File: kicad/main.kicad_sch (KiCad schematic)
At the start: 35 parts, among them J1 Jack-DC, J2 LCD_Out, J3 LCD_Light, J4 VIA_A, J5 VIA_B, J6 VIA_Power, SW1 Step, SW2 Reset, X1 1 MHz

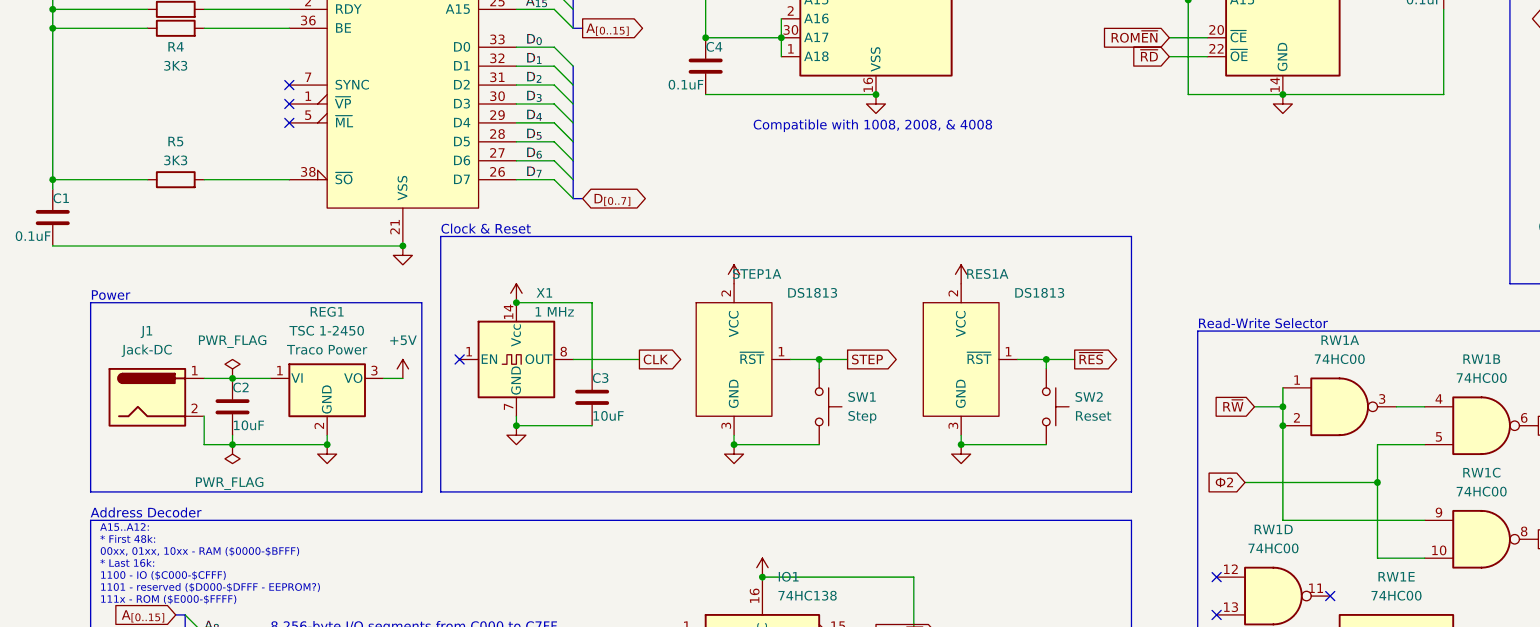
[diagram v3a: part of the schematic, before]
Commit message: Add LEDs
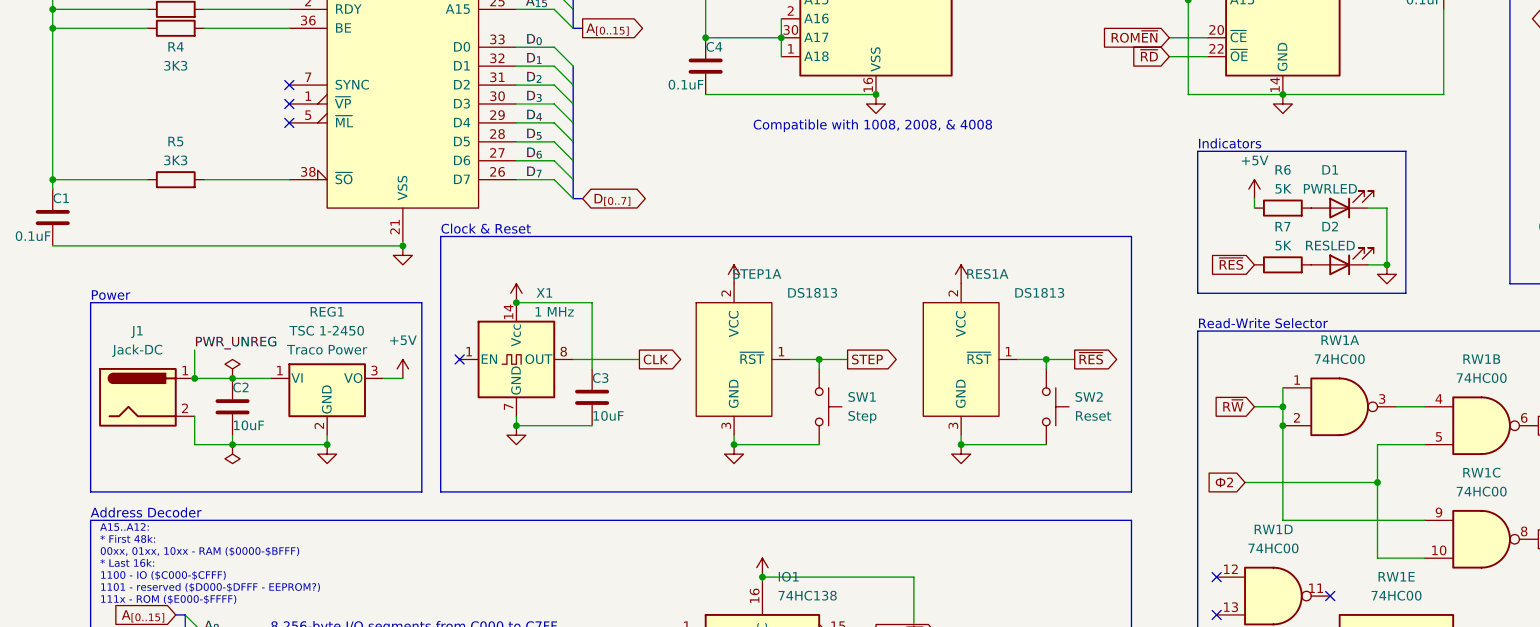
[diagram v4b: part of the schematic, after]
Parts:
- added D1: PWRLED, LED_THT:LED_D3.0mm, symbol Device:LED
- added D2: RESLED, LED_THT:LED_D3.0mm, symbol Device:LED
- added R6, R7: 5K, Resistor_THT:R_Axial_DIN0204_L3.6mm_D1.6mm_P7.62mm_Horizontal, symbol Device:R
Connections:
- net +5V: now also R6.1
- net GND: now also D1.1 (K), D2.1 (K)
- net ~{RES}: now also R7.1
- net PWR_UNREG: now reaches C2.1, J1.1, REG1.1 (VI)
- new net: D1.2 (A), R6.2
- new net: D2.2 (A), R7.2
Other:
- note added: "Indicators"
- moved on the sheet: J1

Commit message: V08
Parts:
- removed J2: LCD_Out, Connector_PinHeader_2.54mm:PinHeader_1x14_P2.54mm_Vertical, symbol Connector:Conn_01x14_Male
- removed J3: LCD_Light, Connector_PinHeader_2.54mm:PinHeader_1x02_P2.54mm_Vertical, symbol Connector:Conn_01x02_Male
- removed J4: VIA_A, Connector_PinHeader_2.54mm:PinHeader_2x05_P2.54mm_Vertical, symbol Connector:Conn_01x10_Male
- removed J5: VIA_B, Connector_PinHeader_2.54mm:PinHeader_2x05_P2.54mm_Vertical, symbol Connector:Conn_01x10_Male
- removed J6: VIA_Power, Connector_PinHeader_2.54mm:PinHeader_1x02_P2.54mm_Vertical, symbol Connector:Conn_01x02_Male
- added J2: LCD, Connector_PinHeader_2.54mm:PinHeader_1x16_P2.54mm_Vertical, symbol Connector:Conn_01x16_Male
- added J3: VIA_A, Connector_PinHeader_2.54mm:PinHeader_2x07_P2.54mm_Vertical, symbol Connector:Conn_01x14_Male
- added J4: VIA_B, Connector_PinHeader_2.54mm:PinHeader_2x07_P2.54mm_Vertical, symbol Connector:Conn_01x14_Male
- D1: value PWRLED -> PWR
- D2: value RESLED -> RES
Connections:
- net +5V: now also J2.15 (Pin_15), J2.2 (Pin_2), J3.14 (Pin_14), J3.2 (Pin_2), J4.14 (Pin_14), J4.2 (Pin_2)
- net A_{0}: now also J2.4 (Pin_4)
- net D_{0}: now also J2.7 (Pin_7)
- net D_{1}: now also J2.8 (Pin_8)
- net D_{2}: now also J2.9 (Pin_9)
- net D_{3}: now also J2.10 (Pin_10)
- net D_{4}: now also J2.11 (Pin_11)
- net D_{5}: now also J2.12 (Pin_12)
- net D_{6}: now also J2.13 (Pin_13)
- net D_{7}: now also J2.14 (Pin_14)
- net GND: now also J2.1 (Pin_1), J2.16 (Pin_16), J3.1 (Pin_1), J3.13 (Pin_13), J4.1 (Pin_1), J4.13 (Pin_13)
- net LCD~{EN}: now also J2.6 (Pin_6)
- net ~{WD}: now also J2.5 (Pin_5)
- net at RV1.2: now also J2.3 (Pin_3)
- net at VIA1.2 (PA0): now also J3.3 (Pin_3)
- net at VIA1.39 (CA2): now also J3.12 (Pin_12)
- net at VIA1.3 (PA1): now also J3.4 (Pin_4)
- net at VIA1.4 (PA2): now also J3.5 (Pin_5)
- net at VIA1.5 (PA3): now also J3.6 (Pin_6)
- net at VIA1.6 (PA4): now also J3.7 (Pin_7)
- net at VIA1.7 (PA5): now also J3.8 (Pin_8)
- net at VIA1.8 (PA6): now also J3.9 (Pin_9)
- net at VIA1.9 (PA7): now also J3.10 (Pin_10)
- net at VIA1.40 (CA1): now also J3.11 (Pin_11)
- net at VIA1.10 (PB0): now also J4.3 (Pin_3)
- net at VIA1.19 (CB2): now also J4.12 (Pin_12)
- net at VIA1.11 (PB1): now also J4.4 (Pin_4)
- net at VIA1.12 (PB2): now also J4.5 (Pin_5)
- net at VIA1.13 (PB3): now also J4.6 (Pin_6)
- net at VIA1.14 (PB4): now also J4.7 (Pin_7)
- net at VIA1.15 (PB5): now also J4.8 (Pin_8)
- net at VIA1.16 (PB6): now also J4.9 (Pin_9)
- net at VIA1.17 (PB7): now also J4.10 (Pin_10)
- net at VIA1.18 (CB1): now also J4.11 (Pin_11)

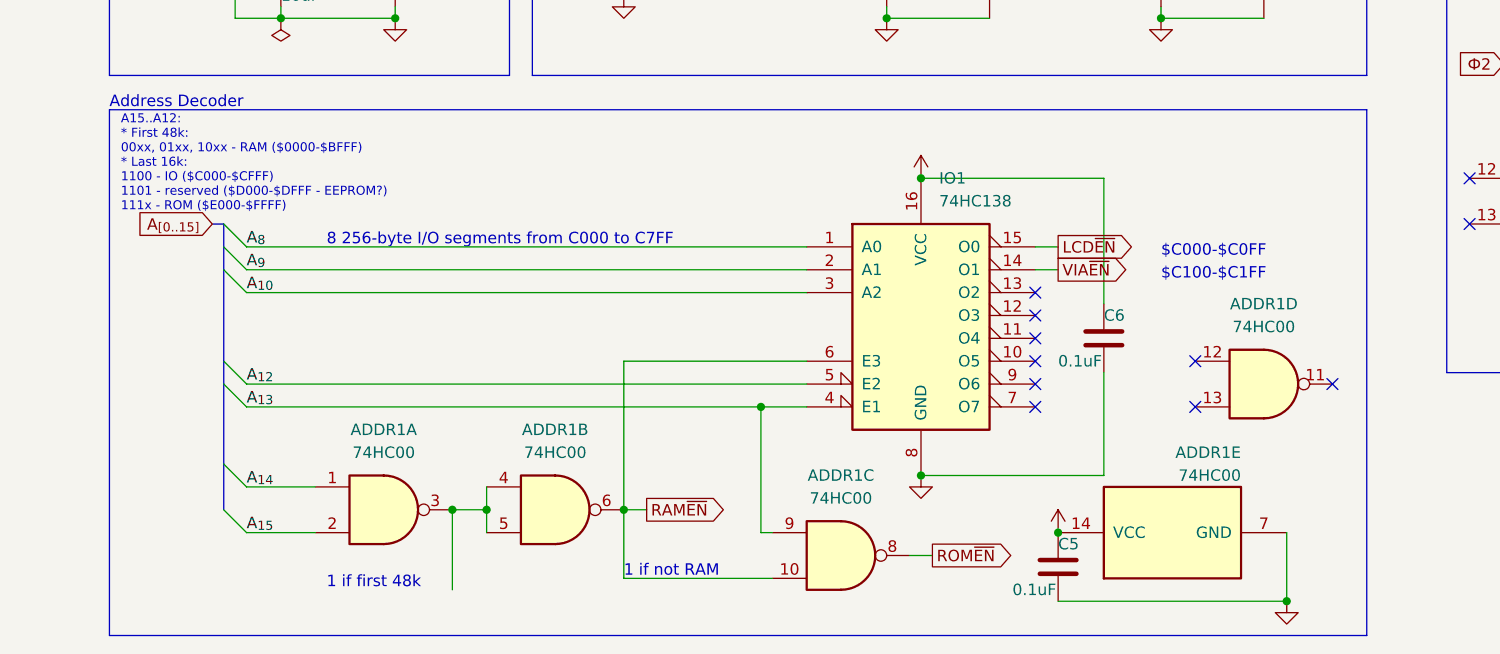
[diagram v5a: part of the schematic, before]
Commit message: Update V8 schematics, move I/O to $Dxxx
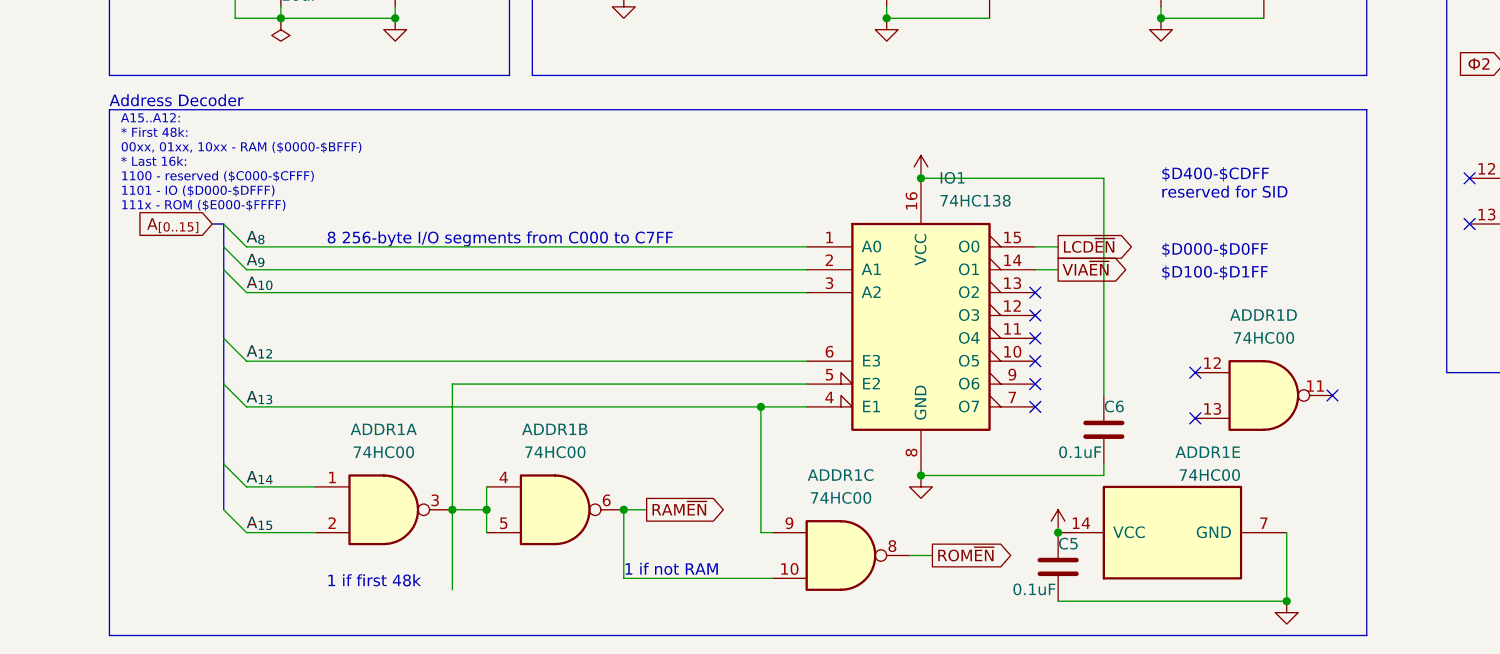
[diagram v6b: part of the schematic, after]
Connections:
- net A_{12}: now also IO1.6 (E3); no longer IO1.5 (E2)
- net RAM~{EN}: no longer IO1.6 (E3)
- net at ADDR1.3, ADDR1.4, ADDR1.5: now also IO1.5 (E2)
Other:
- note added: "$D000-$D0FF"
- note added: "$D100-$D1FF"
- note added: "$D400-$CDFF reserved for SID"
- note added: "A15..A12: * First 48k: 00xx, 01xx, 10xx - RAM ($0000-$BFFF) * Last 16k: 1100 - reserved ($C000-$CFFF) 1101 - IO ($D000-$DFFF) 111x - ROM ($E000-$FFFF)"
- note removed: "$C000-$C0FF"
- note removed: "$C100-$C1FF"
- note removed: "A15..A12: * First 48k: 00xx, 01xx, 10xx - RAM ($0000-$BFFF) * Last 16k: 1100 - IO ($C000-$CFFF) 1101 - reserved ($D000-$DFFF - EEPROM?) 111x - ROM ($E000-$FFFF)"
- moved on the sheet: ADDR1D, C6
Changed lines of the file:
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@@
   (no_connect (at 127 166.37))
   (no_connect (at 50.8 39.37))
-  (no_connect (at 160.02 166.37))
+  (no_connect (at 160.02 167.64))
   (no_connect (at 127 168.91))
-  (no_connect (at 144.78 163.83))
+  (no_connect (at 144.78 165.1))
   (no_connect (at 73.66 114.3))
   (no_connect (at 127 156.21))
   (no_connect (at 50.8 77.47))
-  (no_connect (at 144.78 168.91))
+  (no_connect (at 144.78 170.18))
   (no_connect (at 127 163.83))
   (no_connect (at 50.8 80.01))
@@
     (stroke (width 0) (type default) (color 0 0 0 0))
   )
-  (bus_entry (at 36.83 163.83) (size 2.54 2.54)
+  (bus_entry (at 36.83 161.29) (size 2.54 2.54)
     (stroke (width 0) (type default) (color 0 0 0 0))
   )
@@
     (stroke (width 0.75) (type default) (color 0 0 0 0))
   )
-  (wire (pts (xy 269.24 151.13) (xy 260.35 151.13))
+  (wire (pts (xy 62.23 166.37) (xy 62.23 180.34))
     (stroke (width 0) (type default) (color 0 0 0 0))
   )
-  (wire (pts (xy 81.28 163.83) (xy 81.28 180.34))
+  (wire (pts (xy 269.24 151.13) (xy 260.35 151.13))
     (stroke (width 0) (type default) (color 0 0 0 0))
   )
@@
     (stroke (width 0) (type default) (color 0 0 0 0))
   )
-  (wire (pts (xy 81.28 163.83) (xy 101.6 163.83))
-    (stroke (width 0) (type default) (color 0 0 0 0))
-  )
   (wire (pts (xy 234.95 53.34) (xy 229.87 53.34))
     (stroke (width 0) (type default) (color 0 0 0 0))
@@
     (stroke (width 0) (type default) (color 0 0 0 0))
   )
+  (wire (pts (xy 62.23 166.37) (xy 101.6 166.37))
+    (stroke (width 0) (type default) (color 0 0 0 0))
+  )
   (wire (pts (xy 96.52 182.88) (xy 97.79 182.88))
     (stroke (width 0) (type default) (color 0 0 0 0))
@@
     (stroke (width 0) (type default) (color 0 0 0 0))
   )
-  (wire (pts (xy 39.37 166.37) (xy 101.6 166.37))
+  (wire (pts (xy 39.37 163.83) (xy 101.6 163.83))
     (stroke (width 0) (type default) (color 0 0 0 0))
   )
@@
     (stroke (width 0) (type default) (color 0 0 0 0))
   )
-  (bus (pts (xy 36.83 163.83) (xy 36.83 166.37))
+  (bus (pts (xy 36.83 161.29) (xy 36.83 166.37))
     (stroke (width 0.75) (type default) (color 0 0 0 0))
   )
@@
     (stroke (width 0) (type default) (color 0 0 0 0))
   )
-  (wire (pts (xy 134.62 157.48) (xy 134.62 143.51))
+  (wire (pts (xy 134.62 167.64) (xy 134.62 143.51))
     (stroke (width 0) (type default) (color 0 0 0 0))
   )
@@
     (stroke (width 0) (type default) (color 0 0 0 0))
   )
-  (bus (pts (xy 36.83 153.67) (xy 36.83 163.83))
+  (bus (pts (xy 36.83 153.67) (xy 36.83 161.29))
     (stroke (width 0.75) (type default) (color 0 0 0 0))
   )
@@
     (stroke (width 0.75) (type default) (color 0 0 0 0))
   )
-  (wire (pts (xy 134.62 165.1) (xy 134.62 176.53))
+  (wire (pts (xy 134.62 175.26) (xy 134.62 176.53))
     (stroke (width 0) (type default) (color 0 0 0 0))
   )
@@
     (effects (font (size 1.27 1.27)) (justify left bottom))
   )
-  (text "$C100-$C1FF" (at 140.97 154.94 0)
+  (text "$D100-$D1FF" (at 140.97 154.94 0)
     (effects (font (size 1.27 1.27)) (justify left bottom))
   )
-  (text "A15..A12:\n* First 48k:\n00xx, 01xx, 10xx - RAM ($0000-$BFFF)\n* Last 16k:\n1100 - IO ($C000-$CFFF)\n1101 - reserved ($D000-$DFFF - EEPROM?)\n111x - ROM ($E000-$FFFF)"
+  (text "A15..A12:\n* First 48k:\n00xx, 01xx, 10xx - RAM ($0000-$BFFF)\n* Last 16k:\n1100 - reserved ($C000-$CFFF)\n1101 - IO ($D000-$DFFF)\n111x - ROM ($E000-$FFFF)"
     (at 25.4 147.32 0)
     (effects (font (size 1 1)) (justify left bottom))
@@
     (effects (font (size 1.27 1.27)) (justify left bottom))
   )
-  (text "$C000-$C0FF" (at 140.97 152.4 0)
+  (text "$D000-$D0FF" (at 140.97 152.4 0)
     (effects (font (size 1.27 1.27)) (justify left bottom))
   )
@@
     (effects (font (size 1.27 1.27)) (justify left bottom))
   )
+  (text "$D400-$CDFF\nreserved for SID" (at 140.97 146.05 0)
+    (effects (font (size 1.27 1.27)) (justify left bottom))
+  )
   (label "A_{7}" (at 113.03 45.72 0)
     (effects (font (size 1.27 1.27)) (justify left bottom))
@@
     (effects (font (size 1.27 1.27)) (justify left bottom))
   )
-  (label "A_{12}" (at 39.37 166.37 0)
+  (label "A_{12}" (at 39.37 163.83 0)
     (effects (font (size 1.27 1.27)) (justify left bottom))
   )
@@
     (pin "7")
   )
-  (symbol (lib_id "74xx:74HC00") (at 152.4 166.37 0) (unit 4)
+  (symbol (lib_id "74xx:74HC00") (at 152.4 167.64 0) (unit 4)
     (in_bom yes) (on_board yes) (fields_autoplaced)
-    (property "Reference" "ADDR1" (id 0) (at 152.4 157.48 0))
-    (property "Value" "74HC00" (id 1) (at 152.4 160.02 0))
-    (property "Footprint" "Package_DIP:DIP-14_W7.62mm" (id 2) (at 152.4 166.37 0)
+    (property "Reference" "ADDR1" (id 0) (at 152.4 158.75 0))
+    (property "Value" "74HC00" (id 1) (at 152.4 161.29 0))
+    (property "Footprint" "Package_DIP:DIP-14_W7.62mm" (id 2) (at 152.4 167.64 0)
       (effects (font (size 1.27 1.27)) hide)
     )
-    (property "Datasheet" "http://www.ti.com/lit/gpn/sn74hc00" (id 3) (at 152.4 166.37 0)
+    (property "Datasheet" "http://www.ti.com/lit/gpn/sn74hc00" (id 3) (at 152.4 167.64 0)
       (effects (font (size 1.27 1.27)) hide)
     )
@@
     (pin "7")
   )
-  (symbol (lib_id "Device:C") (at 134.62 161.29 0) (unit 1)
+  (symbol (lib_id "Device:C") (at 134.62 171.45 0) (unit 1)
     (in_bom yes) (on_board yes)
-    (property "Reference" "C6" (id 0) (at 134.62 158.75 0)
+    (property "Reference" "C6" (id 0) (at 134.62 168.91 0)
       (effects (font (size 1.27 1.27)) (justify left))
     )
-    (property "Value" "0.1uF" (id 1) (at 129.54 163.83 0)
+    (property "Value" "0.1uF" (id 1) (at 129.54 173.99 0)
       (effects (font (size 1.27 1.27)) (justify left))
     )
-    (property "Footprint" "Capacitor_THT:C_Disc_D3.0mm_W2.0mm_P2.50mm" (id 2) (at 135.5852 165.1 0)
+    (property "Footprint" "Capacitor_THT:C_Disc_D3.0mm_W2.0mm_P2.50mm" (id 2) (at 135.5852 175.26 0)
       (effects (font (size 1.27 1.27)) hide)
     )
-    (property "Datasheet" "~" (id 3) (at 134.62 161.29 0)
+    (property "Datasheet" "~" (id 3) (at 134.62 171.45 0)
       (effects (font (size 1.27 1.27)) hide)
     )

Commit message: V9 & GAL stuff
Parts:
- added J3: Addr, Connector_PinHeader_2.54mm:PinHeader_1x08_P2.54mm_Vertical, symbol Connector:Conn_01x08_Male
- added J4: IO~{EN}_{[2..7]}, Connector_PinHeader_2.54mm:PinHeader_2x03_P2.54mm_Vertical, symbol Connector:Conn_01x06_Male
- added J5: Data, Connector_PinHeader_2.54mm:PinHeader_1x08_P2.54mm_Vertical, symbol Connector:Conn_01x08_Male
- added J6: Control, Connector_PinHeader_2.54mm:PinHeader_2x05_P2.54mm_Vertical, symbol Connector:Conn_01x10_Male
- C3: value 10uF -> 0,1uF
- renumbered C6 to C4, C4 to C5, C5 to C6, J3 to J7, J4 to J8
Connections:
- net +5V: now also C3.2, C4.2, J7.13 (Pin_13), J8.13 (Pin_13), J6.2 (Pin_2), J6.9 (Pin_9); no longer C3.1, C4.1, J7.14 (Pin_14), J8.14 (Pin_14)
- net A_{0}: now also J3.1 (Pin_1)
- net A_{1}: now also J3.2 (Pin_2)
- net A_{2}: now also J3.3 (Pin_3)
- net A_{3}: now also J3.4 (Pin_4)
- net A_{4}: now also J3.5 (Pin_5)
- net A_{5}: now also J3.6 (Pin_6)
- net A_{6}: now also J3.7 (Pin_7)
- net A_{7}: now also J3.8 (Pin_8)
- net D_{0}: now also J5.1 (Pin_1)
- net D_{1}: now also J5.2 (Pin_2)
- net D_{2}: now also J5.3 (Pin_3)
- net D_{3}: now also J5.4 (Pin_4)
- net D_{4}: now also J5.5 (Pin_5)
- net D_{5}: now also J5.6 (Pin_6)
- net D_{6}: now also J5.7 (Pin_7)
- net D_{7}: now also J5.8 (Pin_8)
- net GND: now also C3.1, C4.1, J7.14 (Pin_14), J8.14 (Pin_14), J6.1 (Pin_1), J6.10 (Pin_10); no longer C3.2, C4.2, J7.13 (Pin_13), J8.13 (Pin_13)
- net R~{W}: now also J6.3 (Pin_3)
- net ~{IRQ}: now also J6.7 (Pin_7)
- net ~{RD}: now also J6.4 (Pin_4)
- net ~{RES}: now also J6.8 (Pin_8)
- net ~{WD}: now also J6.5 (Pin_5)
- net Ф2: now also J6.6 (Pin_6)
- net IO~{EN}_{5}: now reaches IO1.10 (O5)
- net IO~{EN}_{5}: now also J4.4 (Pin_4)
- net IO~{EN}_{4}: now reaches IO1.11 (O4)
- net IO~{EN}_{4}: now also J4.3 (Pin_3)
- net IO~{EN}_{3}: now reaches IO1.12 (O3)
- net IO~{EN}_{3}: now also J4.2 (Pin_2)
- net IO~{EN}_{2}: now reaches IO1.13 (O2)
- net IO~{EN}_{2}: now also J4.1 (Pin_1)
- net IO~{EN}_{7}: now reaches IO1.7 (O7)
- net IO~{EN}_{7}: now also J4.6 (Pin_6)
- net IO~{EN}_{6}: now reaches IO1.9 (O6)
- net IO~{EN}_{6}: now also J4.5 (Pin_5)
- no-connect marks 17 -> 11
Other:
- note added: "Expansion"
- moved on the sheet: ADDR1A, ADDR1B, ADDR1C, ADDR1D, ADDR1E, C2, C3, C4, C5, C6, C7, C8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
